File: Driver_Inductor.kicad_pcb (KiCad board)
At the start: 6 copper layers, 119.6 x 60.5 mm, 91 parts, among them J1 Control_A, J2 DC+, J3 DC-, J4 OUT1, J5 OUT2, Q1 IRLML2402TRPBF, U3 LM1117GS-5.0, U4 LMV7219M5, U5 ADuM1200AR

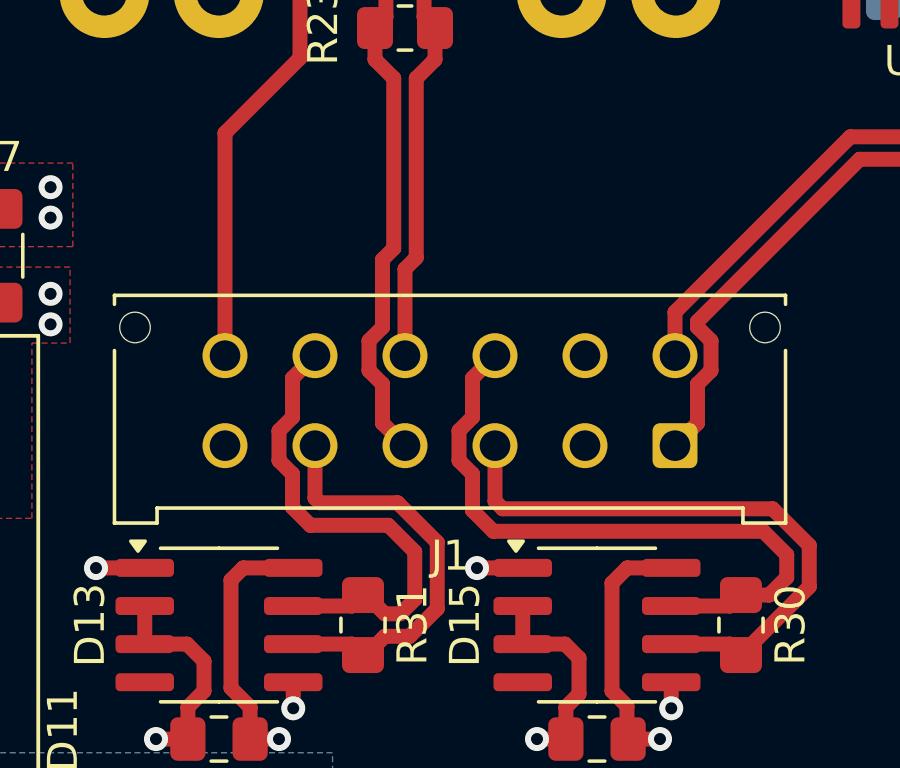
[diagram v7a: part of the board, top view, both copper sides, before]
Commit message: Изменения: изменил BOM, сделал заказ
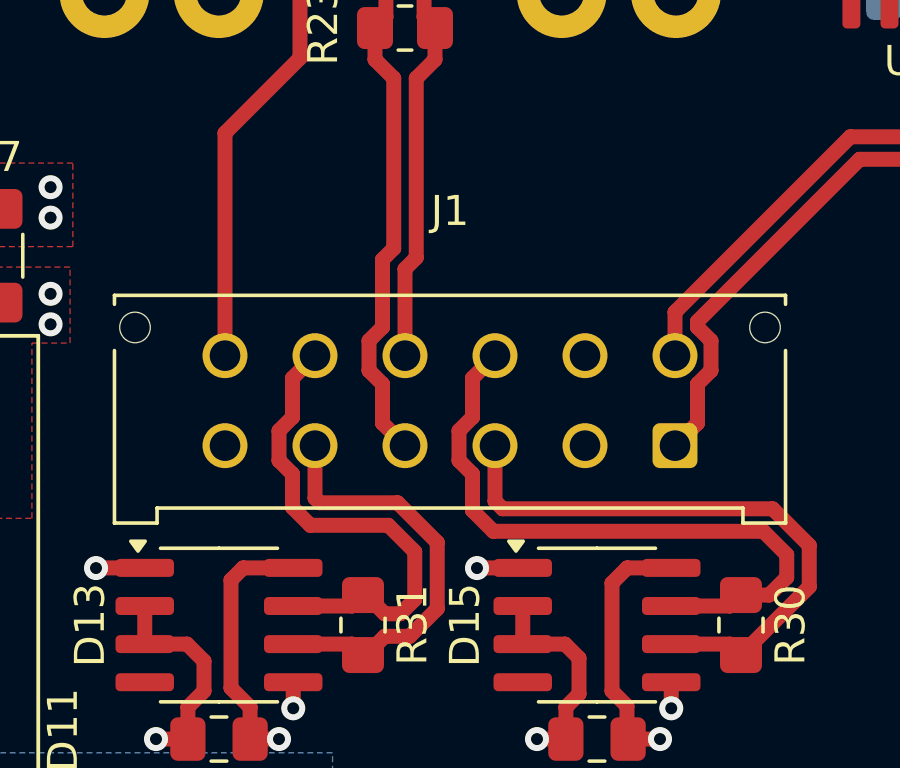
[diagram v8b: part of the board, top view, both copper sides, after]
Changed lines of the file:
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@@
 		(tags "capacitor handsolder")
 		(property "Reference" "C9"
-			(at 0 -1.68 360)
+			(at 0 -1.68 0)
 			(layer "F.SilkS")
 			(effects
@@
 		)
 		(property "Value" "2.2u"
-			(at 0 1.68 360)
+			(at 0 1.68 0)
 			(layer "F.Fab")
 			(effects
@@
 		)
 		(fp_text user "${REFERENCE}"
-			(at 0 0 360)
+			(at 0 0 0)
 			(layer "F.Fab")
 			(effects
@@
 		)
 		(property "Value" "ADM1485JRZ"
-			(at 0 3.4 360)
+			(at 0 3.4 0)
 			(layer "F.Fab")
 			(effects
@@
 		)
 		(fp_text user "${REFERENCE}"
-			(at 0 0 360)
+			(at 0 0 0)
 			(layer "F.Fab")
 			(effects
@@
 		(tags "capacitor handsolder")
 		(property "Reference" "C11"
-			(at 0 -1.6 360)
+			(at 0 -1.6 0)
 			(layer "F.SilkS")
 			(effects
@@
 		)
 		(property "Value" "2.2u"
-			(at 0 1.68 360)
+			(at 0 1.68 0)
 			(layer "F.Fab")
 			(effects
@@
 		)
 		(fp_text user "${REFERENCE}"
-			(at 0 0 360)
+			(at 0 0 0)
 			(layer "F.Fab")
 			(effects
@@
 		(tags "connector Molex Micro-Fit_3.0 vertical")
 		(property "Reference" "J1"
-			(at 7.5 -3.67 0)
+			(at 7.5 7.82 0)
 			(layer "F.SilkS")
 			(effects
